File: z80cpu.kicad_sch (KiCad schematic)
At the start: 11 parts

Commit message: Notes in kicad's sheet text blocks
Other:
- company: (none) -> Logic Systems Int'l Inc
- title: (none) -> CEDA - Sanco 8003 schematics
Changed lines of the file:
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@@
 (kicad_sch (version 20230121) (generator eeschema)
   (paper "A4")
+  (title_block
+    (title "CEDA - Sanco 8003 schematics")
+    (rev "05")
+    (company "Logic Systems Int'l Inc")
+    (comment 1 "reversed by RetrOfficina - retrofficina.glgprograms.it")
+    (comment 3 "The CPU and some collateral signals")
+    (comment 4 "Z80")
+  )
   (junction (at 182.88 54.61) (diameter 0) (color 0 0 0 0)
   )

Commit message: drc: corrections in net names
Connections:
- net ioreq is gone; now on net ~{ioreq}: UF2.20 (~{IORQ})
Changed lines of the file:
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@@
 		)
 	)
-	(label "ioreq"
+	(label "~{ioreq}"
 		(at 88.9 92.71 0)
 		(effects

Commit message: drc: fixed labels
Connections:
- net IO_OE renamed ~{IO_OE}
- net IO_WR renamed ~{IO_WR}
- net MEM_WR renamed ~{MEM_WR}
- net ~{IOREQ} renamed ~{IORQ}
- net ~{ioreq} renamed ~{iorq}
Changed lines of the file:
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@@
 		)
 	)
-	(label "~{ioreq}"
+	(label "~{iorq}"
 		(at 74.93 76.2 180)
 		(effects
@@
 		)
 	)
-	(label "~{ioreq}"
+	(label "~{iorq}"
 		(at 88.9 92.71 0)
 		(effects
@@
 		)
 	)
-	(label "~{IOREQ}"
+	(label "~{IORQ}"
 		(at 17.78 30.48 0)
 		(effects
@@
 		)
 	)
-	(label "~{IOREQ}"
+	(label "~{IORQ}"
 		(at 22.86 156.21 0)
 		(effects
@@
 		)
 	)
-	(label "~{IOREQ}"
+	(label "~{IORQ}"
 		(at 109.22 156.21 0)
 		(effects
@@
 		)
 	)
-	(global_label "MEM_WR"
+	(global_label "~{MEM_WR}"
 		(shape output)
 		(at 157.48 173.99 0)
@@
 		)
 	)
-	(global_label "IO_WR"
+	(global_label "~{IO_WR}"
 		(shape output)
 		(at 157.48 158.75 0)
@@
 		)
 	)
-	(global_label "IO_OE"
+	(global_label "~{IO_OE}"
 		(shape output)
 		(at 71.12 158.75 0)
@@
 		)
 	)
-	(global_label "~{IOREQ}"
+	(global_label "~{IORQ}"
 		(shape output)
 		(at 34.29 76.2 180)

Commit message: Assigned default footprints to ICs
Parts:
- UF2: footprint (none) -> Package_DIP:DIP-40_W15.24mm
- UF6, UH2, UH3: footprint (none) -> Package_DIP:DIP-20_W7.62mm
- UF7, UH1: footprint (none) -> Package_DIP:DIP-14_W7.62mm
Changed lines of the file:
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@@
 			)
 		)
-		(property "Footprint" ""
+		(property "Footprint" "Package_DIP:DIP-14_W7.62mm"
 			(at 137.16 173.99 0)
 			(effects
@@
 			)
 		)
-		(property "Footprint" ""
+		(property "Footprint" "Package_DIP:DIP-14_W7.62mm"
 			(at 50.8 173.99 0)
 			(effects
@@
 			)
 		)
-		(property "Footprint" ""
+		(property "Footprint" "Package_DIP:DIP-20_W7.62mm"
 			(at 198.12 41.91 0)
 			(effects
@@
 			)
 		)
-		(property "Footprint" ""
+		(property "Footprint" "Package_DIP:DIP-40_W15.24mm"
 			(at 115.57 62.23 0)
 			(effects
@@
 			)
 		)
-		(property "Footprint" ""
+		(property "Footprint" "Package_DIP:DIP-14_W7.62mm"
 			(at 209.55 153.67 0)
 			(effects
@@
 			)
 		)
-		(property "Footprint" ""
+		(property "Footprint" "Package_DIP:DIP-20_W7.62mm"
 			(at 198.12 99.06 0)
 			(effects
@@
 			)
 		)
-		(property "Footprint" ""
+		(property "Footprint" "Package_DIP:DIP-20_W7.62mm"
 			(at 54.61 88.9 0)
 			(effects
@@
 			)
 		)
-		(property "Footprint" ""
+		(property "Footprint" "Package_DIP:DIP-14_W7.62mm"
 			(at 134.62 124.46 0)
 			(effects
@@
 			)
 		)
-		(property "Footprint" ""
+		(property "Footprint" "Package_DIP:DIP-14_W7.62mm"
 			(at 105.41 124.46 0)
 			(effects
@@
 			)
 		)
-		(property "Footprint" ""
+		(property "Footprint" "Package_DIP:DIP-14_W7.62mm"
 			(at 50.8 158.75 0)
 			(effects
@@
 			)
 		)
-		(property "Footprint" ""
+		(property "Footprint" "Package_DIP:DIP-14_W7.62mm"
 			(at 137.16 158.75 0)
 			(effects

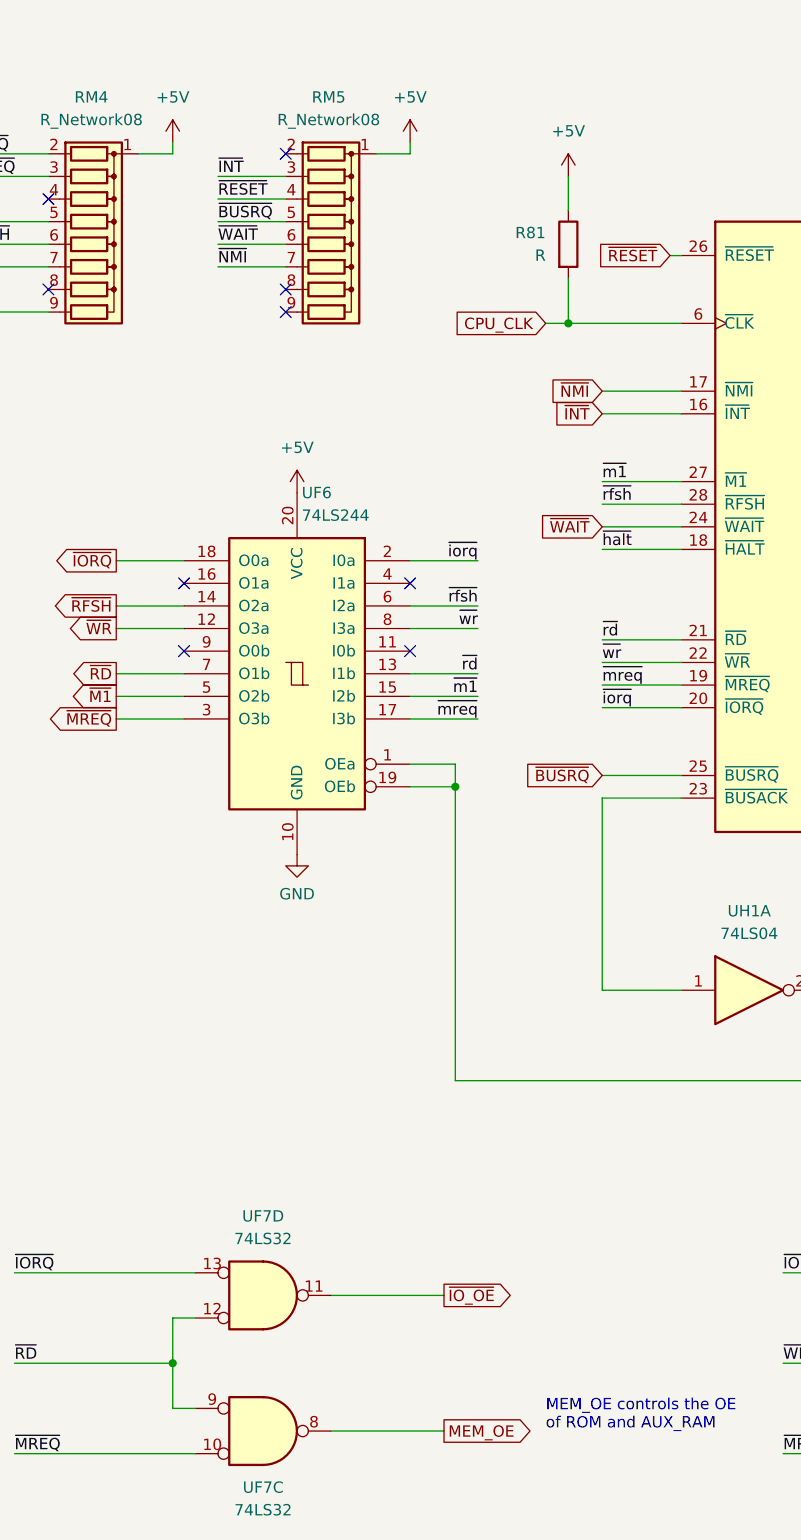
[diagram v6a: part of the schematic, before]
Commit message: Fixed wrong labels and connections, added footprint for dip switch
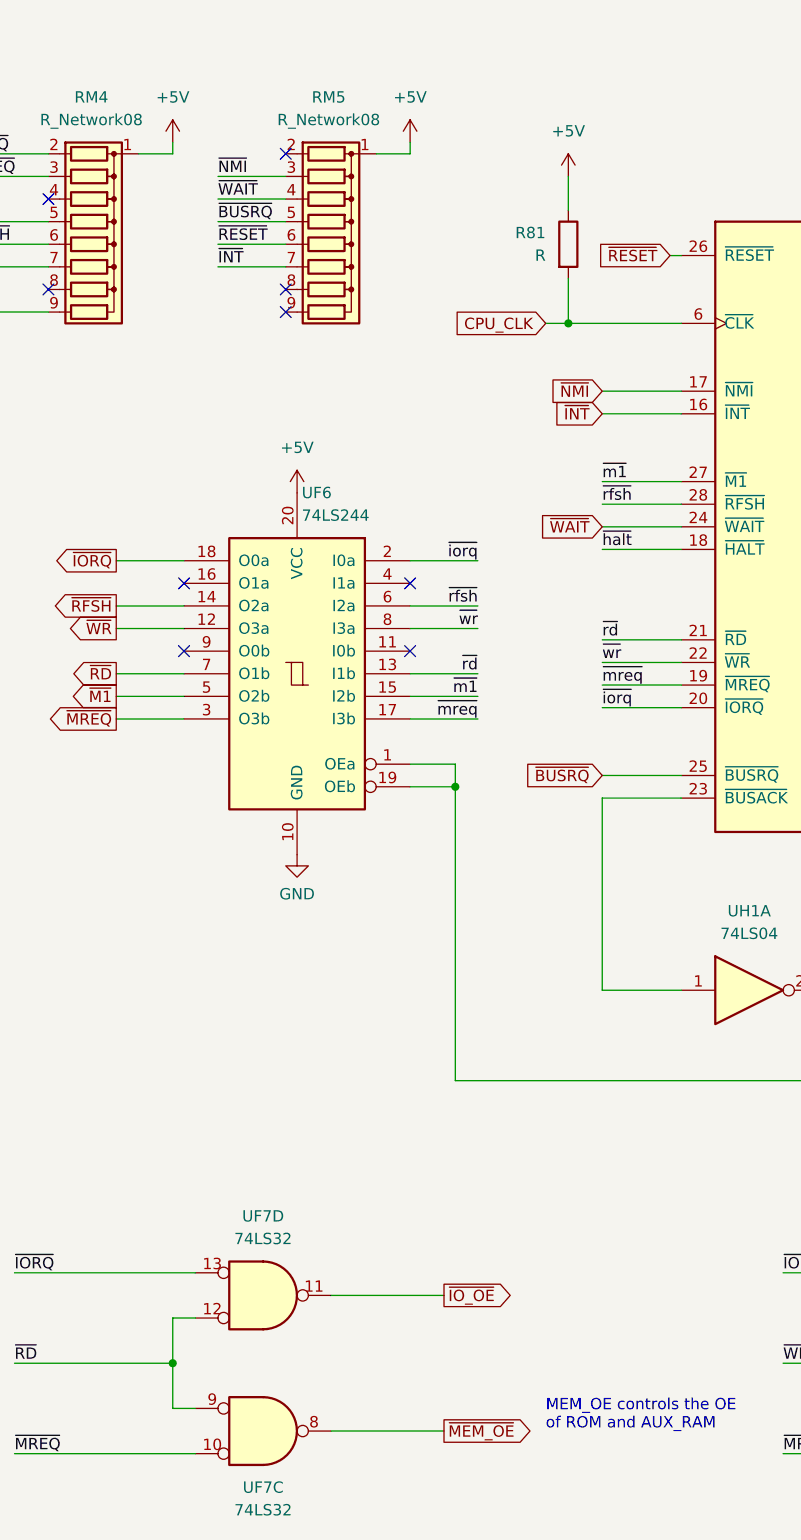
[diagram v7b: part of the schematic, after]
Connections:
- net ~{INT}: now also RM5.7 (R6); no longer RM5.3 (R2)
- net ~{NMI}: now also RM5.3 (R2); no longer RM5.7 (R6)
- net ~{RESET}: now also RM5.6 (R5); no longer RM5.4 (R3)
- net ~{WAIT}: now also RM5.4 (R3); no longer RM5.6 (R5)
- net MEM_OE renamed ~{MEM_OE}

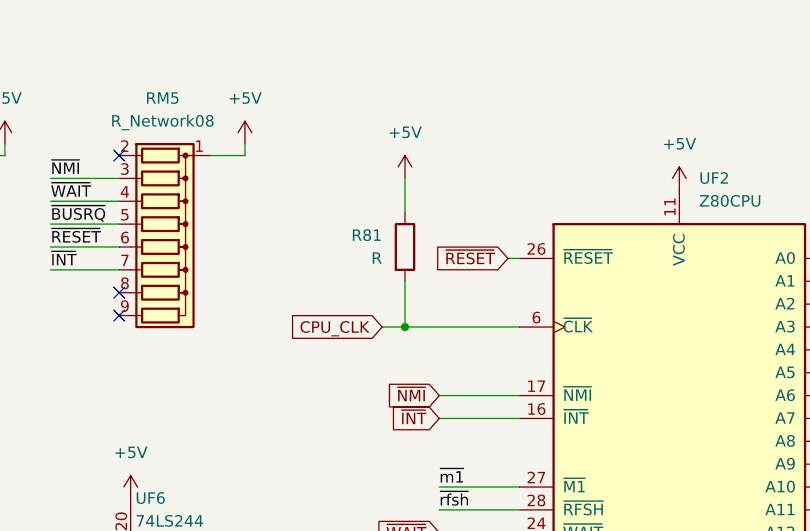
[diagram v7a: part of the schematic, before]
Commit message: pcb: added and placed almost all components
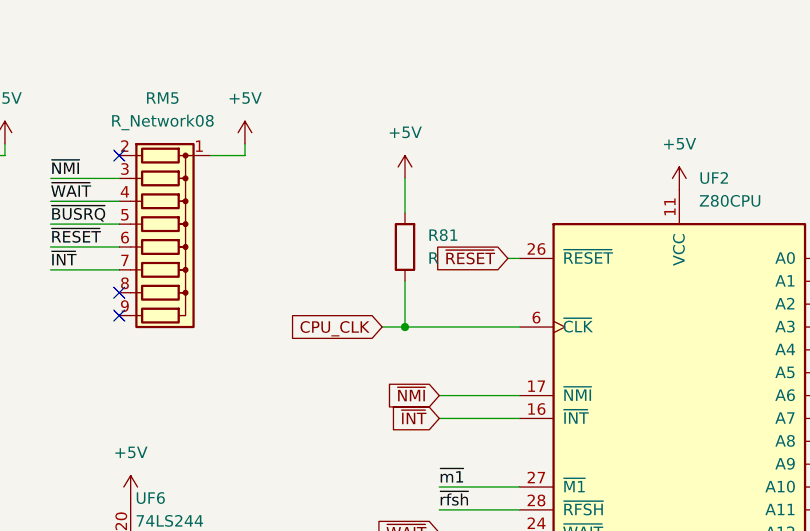
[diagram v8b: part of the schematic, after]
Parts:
- LED1: footprint (none) -> LED_THT:LED_D3.0mm
- R45, R81: footprint (none) -> Resistor_THT:R_Axial_DIN0204_L3.6mm_D1.6mm_P5.08mm_Vertical
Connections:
- net +5V: now also R81.2; no longer R81.1
- net CPU_CLK: now also R81.1; no longer R81.2
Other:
- moved on the sheet: R81
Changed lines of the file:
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@@
 			)
 		)
-		(property "Footprint" ""
+		(property "Footprint" "Resistor_THT:R_Axial_DIN0204_L3.6mm_D1.6mm_P5.08mm_Vertical"
 			(at 238.76 155.448 90)
 			(effects
@@
 			)
 		)
-		(property "Footprint" ""
+		(property "Footprint" "LED_THT:LED_D3.0mm"
 			(at 226.06 153.67 0)
 			(effects
@@
 	(symbol
 		(lib_id "Device:R")
-		(at 85.09 40.64 0)
+		(at 85.09 40.64 180)
 		(unit 1)
 		(exclude_from_sim no)
@@
 		(fields_autoplaced yes)
 		(property "Reference" "R81"
-			(at 82.55 39.37 0)
+			(at 87.63 39.3699 0)
 			(effects
 				(font
@@
 		)
 		(property "Value" "R"
-			(at 82.55 41.91 0)
+			(at 87.63 41.9099 0)
 			(effects
 				(font
@@
 			)
 		)
-		(property "Footprint" ""
-			(at 83.312 40.64 90)
-			(effects
-				(font
+		(property "Footprint" "Resistor_THT:R_Axial_DIN0204_L3.6mm_D1.6mm_P5.08mm_Vertical"
+			(at 86.868 40.64 90)
+			(effects
+				(font
